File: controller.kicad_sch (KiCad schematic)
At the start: 42 parts, among them IC10 NXB0108BQX, IC11 STM32L475RGT6, IC12 W25N512GVEIG, J1 20021121-00014T4LF, J2 10118192-0001LF, Y3 ECS-.327-7-1210-TR

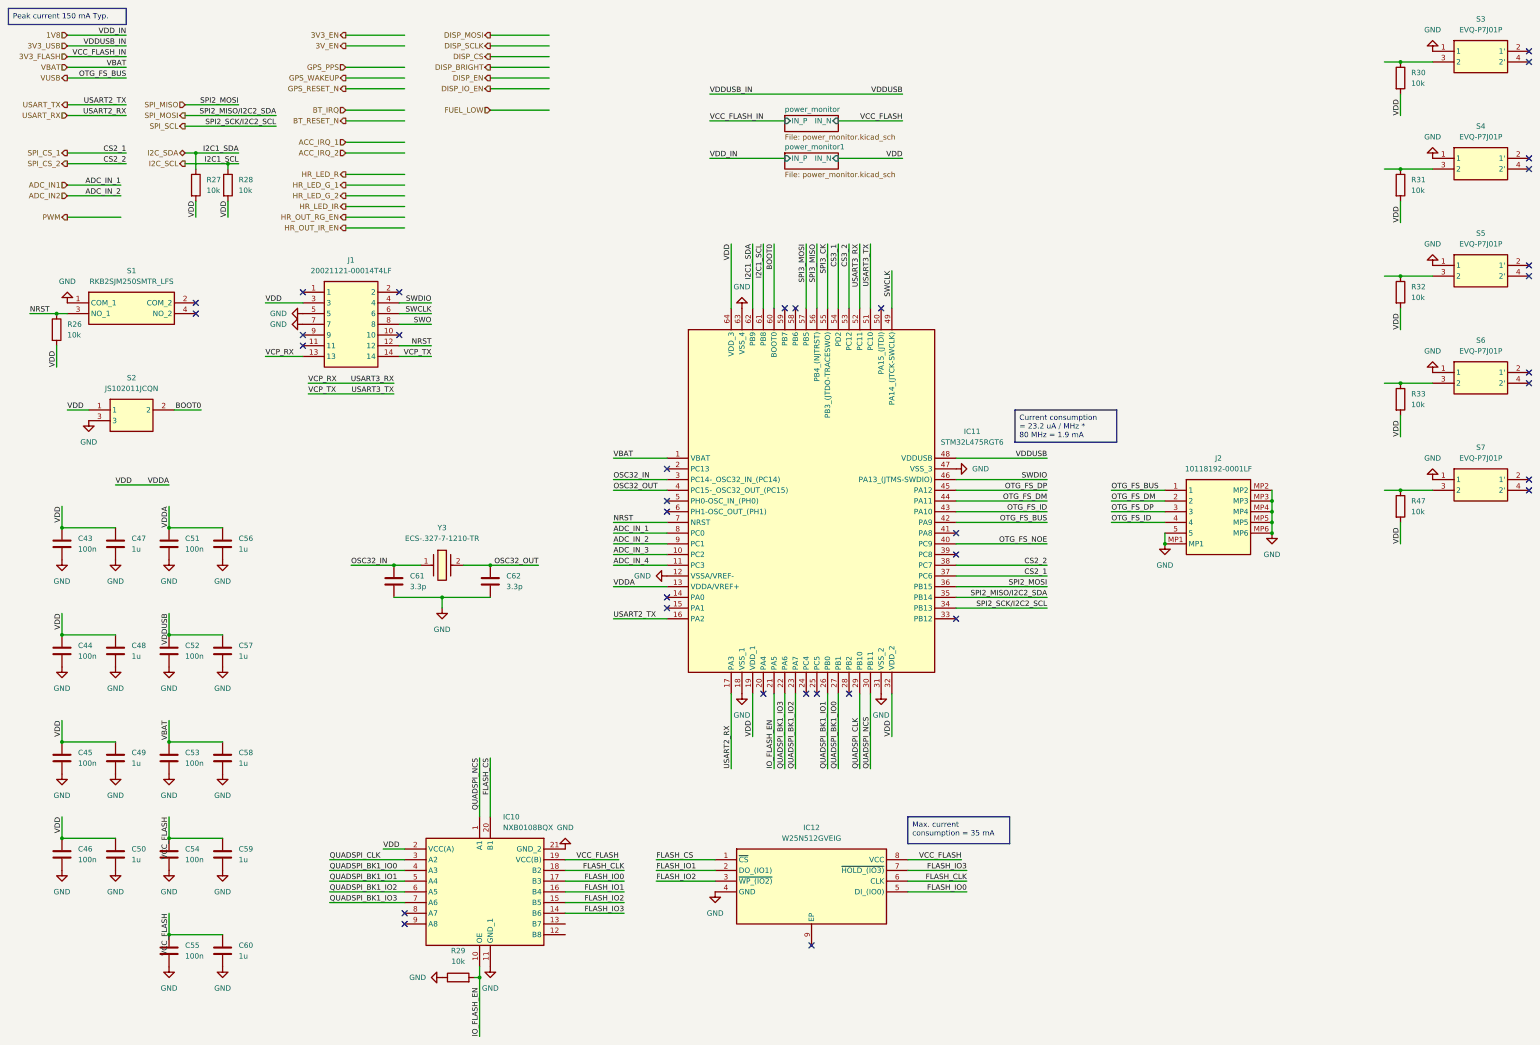
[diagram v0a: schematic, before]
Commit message: Remove BOOT0 switch to 0 ohm resistors
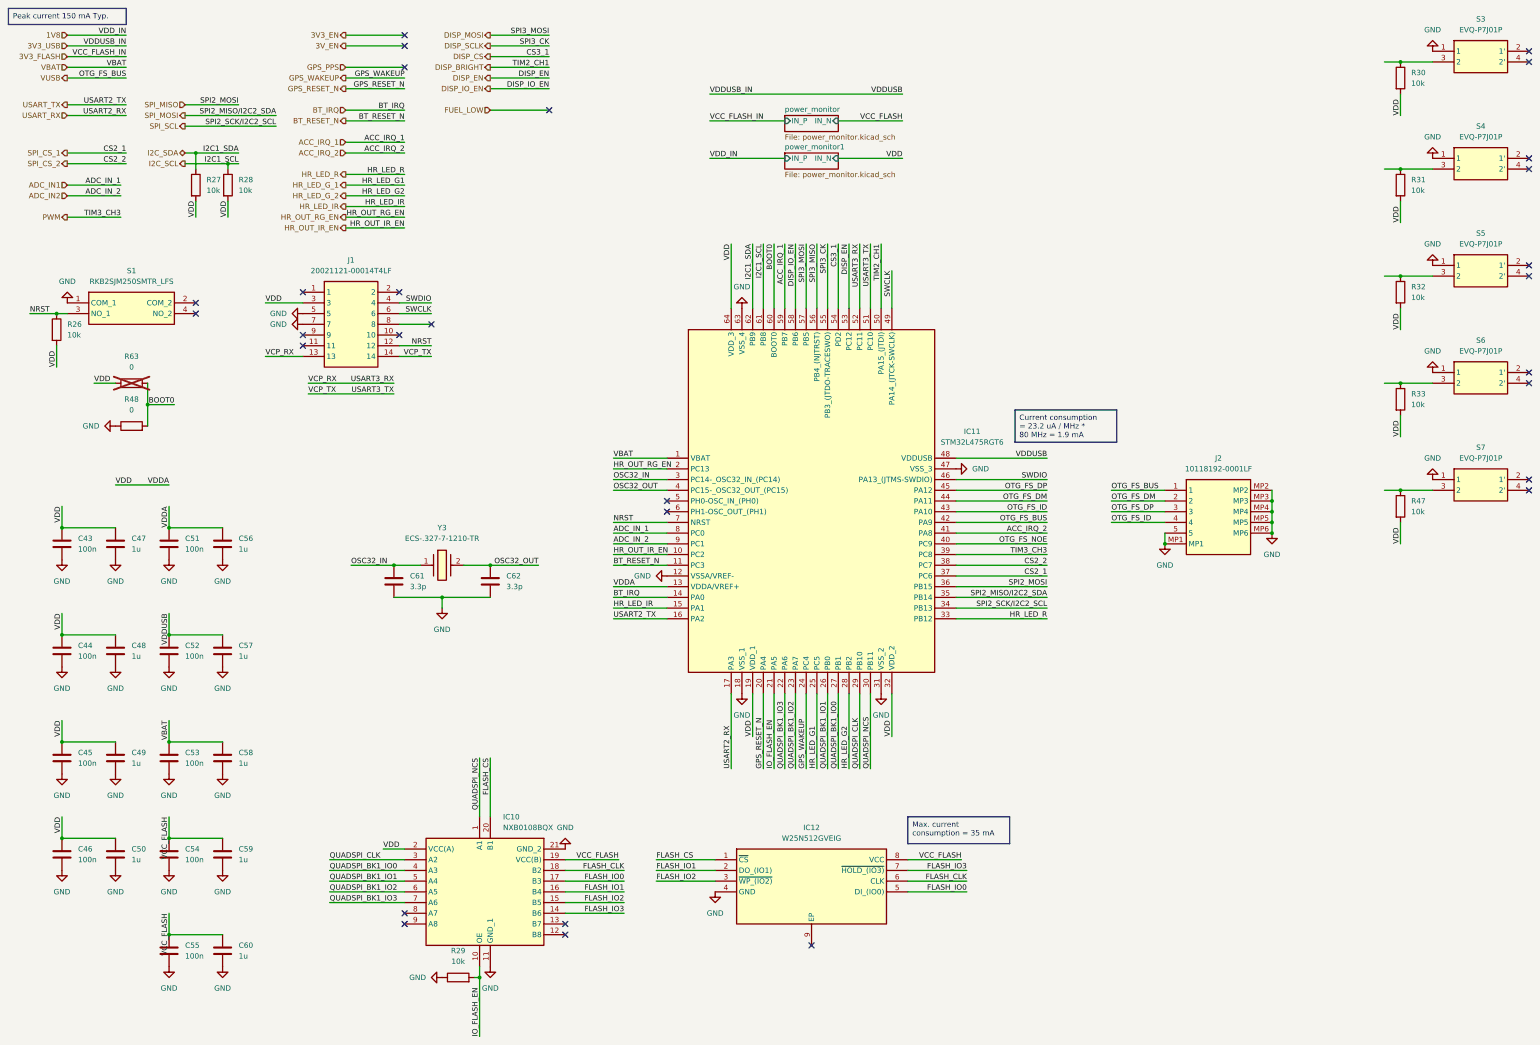
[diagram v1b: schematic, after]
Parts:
- removed S2: JS102011JCQN, JS102011JCQN:JS102011JCQN, symbol JS102011JCQN:JS102011JCQN
- added R48, R63: 0, Resistor_SMD:R_0402_1005Metric_Pad0.72x0.64mm_HandSolder, symbol Device:R
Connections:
- net ADC_IN_3 is gone; now on net HR_OUT_IR_EN: IC11.10 (PC2)
- net ADC_IN_4 is gone; now on net BT_RESET_N: IC11.11 (PC3)
- net CS3_1 is gone; now on net DISP_CS: IC11.54 (PD2)
- net CS3_2 is gone; now on net DISP_EN: IC11.53 (PC12)
- net SPI3_CK is gone; now on net DISP_SCLK: IC11.55 (PB3_(JTDO-TRACESWO))
- net SPI3_MOSI is gone; now on net DISP_MOSI: IC11.57 (PB5)
- net ACC_IRQ_1: now also IC11.59 (PB7)
- net ACC_IRQ_2: now also IC11.41 (PA8)
- net BOOT0: now also R48.2, R63.2
- net BT_IRQ: now also IC11.14 (PA0)
- net DISP_BRIGHT: now also IC11.50 (PA15_(JTDI))
- net DISP_IO_EN: now also IC11.58 (PB6)
- net GND: now also R48.1
- net GPS_RESET_N: now also IC11.20 (PA4)
- net GPS_WAKEUP: now also IC11.24 (PC4)
- net HR_LED_G_1: now also IC11.25 (PC5)
- net HR_LED_G_2: now also IC11.28 (PB2)
- net HR_LED_IR: now also IC11.15 (PA1)
- net HR_LED_R: now also IC11.33 (PB12)
- net HR_OUT_RG_EN: now also IC11.2 (PC13)
- net PWM: now also IC11.39 (PC8)
- net VDD: now also R63.1
- net SWO: no longer names the net of J1.8
- no-connect marks 35 -> 29

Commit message: Finished hardware design
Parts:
- added IC18: PCAL9538ABSHP, QFN50P300X300X100-17N-D, symbol PCAL9538ABSHP:PCAL9538ABSHP
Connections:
- net 1V8: now also J1.3, R30.2, R31.2, R32.2, R33.2, R47.2
- net GND: now also IC12.9 (EP), IC18.15 (A0), IC18.16 (A1), IC18.17 (VSS_2), IC18.6 (VSS_1)
- net HR_LED_G_1: now also IC11.38 (PC7); no longer IC11.25 (PC5)
- net HR_LED_G_2: now also IC11.25 (PC5); no longer IC11.28 (PB2)
- net HR_LED_IR: now also IC11.28 (PB2); no longer IC11.15 (PA1)
- net I2C_SCL: now also IC18.12 (SCL)
- net I2C_SDA: now also IC18.13 (SDA)
- net SPI_CS_2: now also IC11.15 (PA1); no longer IC11.38 (PC7)
- net VBAT: no longer C53.1, C58.1, IC11.1 (VBAT)
- net VDD: now also C53.1, C58.1, IC11.1 (VBAT), IC18.14 (VDD); no longer J1.3, R30.2, R31.2, R32.2, R33.2, R47.2
- net at R31.1, S4.3 (2): now also IC18.2 (P0)
- net at R32.1, S5.3 (2): now also IC18.9 (P6)
- net at R47.1, S7.3 (2): now also IC18.7 (P4)
- net at R33.1, S6.3 (2): now also IC18.8 (P5)
- net at R30.1, S3.3 (2): now also IC18.3 (P1)
- net HR_OUT_RG_EN renamed BTN_INT
- net BTN_INT: now also IC18.11 (~{INT})

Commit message: Remove additional spaces in Manufacturer_Part_Number field
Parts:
- C43, C44, C45, C46, C51, C52, C53, C54, C55: Manufacturer_Part_Number GRM155R71A104MA01D -> GRM155R71A104MA01D
- R26, R27, R28, R29, R30, R31, R32, R33, R47: Manufacturer_Part_Number RC0402JR-0710KP -> RC0402JR-0710KP
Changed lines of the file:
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@@
 			)
 		)
-		(property "Manufacturer_Part_Number" "GRM155R71A104MA01D "
+		(property "Manufacturer_Part_Number" "GRM155R71A104MA01D"
 			(at 63.5 204.47 0)
 			(effects
@@
 			)
 		)
-		(property "Manufacturer_Part_Number" "GRM155R71A104MA01D "
+		(property "Manufacturer_Part_Number" "GRM155R71A104MA01D"
 			(at 63.5 179.07 0)
 			(effects
@@
 			)
 		)
-		(property "Manufacturer_Part_Number" " RC0402JR-0710KP"
+		(property "Manufacturer_Part_Number" "RC0402JR-0710KP"
 			(at 132.08 256.54 0)
 			(effects
@@
 			)
 		)
-		(property "Manufacturer_Part_Number" " RC0402JR-0710KP"
+		(property "Manufacturer_Part_Number" "RC0402JR-0710KP"
 			(at 36.83 102.87 0)
 			(effects
@@
 			)
 		)
-		(property "Manufacturer_Part_Number" " RC0402JR-0710KP"
+		(property "Manufacturer_Part_Number" "RC0402JR-0710KP"
 			(at 355.6 119.38 0)
 			(effects
@@
 			)
 		)
-		(property "Manufacturer_Part_Number" "GRM155R71A104MA01D "
+		(property "Manufacturer_Part_Number" "GRM155R71A104MA01D"
 			(at 38.1 204.47 0)
 			(effects
@@
 			)
 		)
-		(property "Manufacturer_Part_Number" " RC0402JR-0710KP"
+		(property "Manufacturer_Part_Number" "RC0402JR-0710KP"
 			(at 77.47 68.58 0)
 			(effects
@@
 			)
 		)
-		(property "Manufacturer_Part_Number" "GRM155R71A104MA01D "
+		(property "Manufacturer_Part_Number" "GRM155R71A104MA01D"
 			(at 63.5 250.19 0)
 			(effects
@@
 			)
 		)
-		(property "Manufacturer_Part_Number" "GRM155R71A104MA01D "
+		(property "Manufacturer_Part_Number" "GRM155R71A104MA01D"
 			(at 38.1 227.33 0)
 			(effects
@@
 			)
 		)
-		(property "Manufacturer_Part_Number" " RC0402JR-0710KP"
+		(property "Manufacturer_Part_Number" "RC0402JR-0710KP"
 			(at 355.6 68.58 0)
 			(effects
@@
 			)
 		)
-		(property "Manufacturer_Part_Number" "GRM155R71A104MA01D "
+		(property "Manufacturer_Part_Number" "GRM155R71A104MA01D"
 			(at 63.5 227.33 0)
 			(effects
@@
 			)
 		)
-		(property "Manufacturer_Part_Number" " RC0402JR-0710KP"
+		(property "Manufacturer_Part_Number" "RC0402JR-0710KP"
 			(at 355.6 43.18 0)
 			(effects
@@
 			)
 		)
-		(property "Manufacturer_Part_Number" "GRM155R71A104MA01D "
+		(property "Manufacturer_Part_Number" "GRM155R71A104MA01D"
 			(at 63.5 153.67 0)
 			(effects
@@
 			)
 		)
-		(property "Manufacturer_Part_Number" " RC0402JR-0710KP"
+		(property "Manufacturer_Part_Number" "RC0402JR-0710KP"
 			(at 355.6 93.98 0)
 			(effects
@@
 			)
 		)
-		(property "Manufacturer_Part_Number" "GRM155R71A104MA01D "
+		(property "Manufacturer_Part_Number" "GRM155R71A104MA01D"
 			(at 38.1 179.07 0)
 			(effects
@@
 			)
 		)
-		(property "Manufacturer_Part_Number" "GRM155R71A104MA01D "
+		(property "Manufacturer_Part_Number" "GRM155R71A104MA01D"
 			(at 38.1 153.67 0)
 			(effects
@@
 			)
 		)
-		(property "Manufacturer_Part_Number" " RC0402JR-0710KP"
+		(property "Manufacturer_Part_Number" "RC0402JR-0710KP"
 			(at 355.6 144.78 0)
 			(effects
@@
 			)
 		)
-		(property "Manufacturer_Part_Number" " RC0402JR-0710KP"
+		(property "Manufacturer_Part_Number" "RC0402JR-0710KP"
 			(at 69.85 68.58 0)
 			(effects
